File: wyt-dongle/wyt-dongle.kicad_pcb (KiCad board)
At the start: 2 copper layers, 17.2 x 36 mm, 17 parts, among them J1 USB_A, J2 Conn_01x05_Pin, J3 Conn_01x02_Pin, P1 USB_C_Plug_USB2.0, Q1 2N7002, Q2 2N7002, SW1 BOOT, U1 XC6206PxxxMR, U2 ESP32-S2-MINI-2

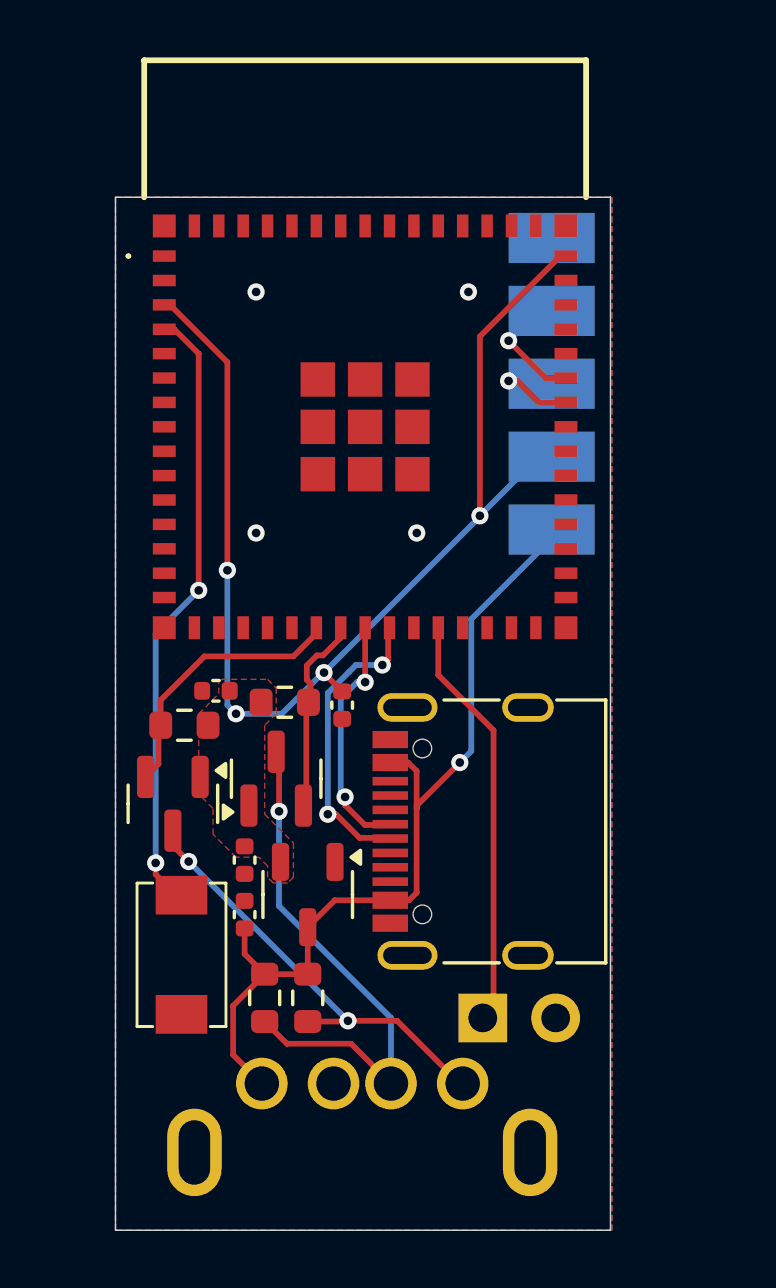
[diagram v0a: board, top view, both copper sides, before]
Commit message: feat: expose more gpios and add reset button
fix: switch to larger LDO

fix: avoid gpio tied to flash for IR LED

fix: connect all usb data pins

fix: add 5.1K resistors for passive usb power
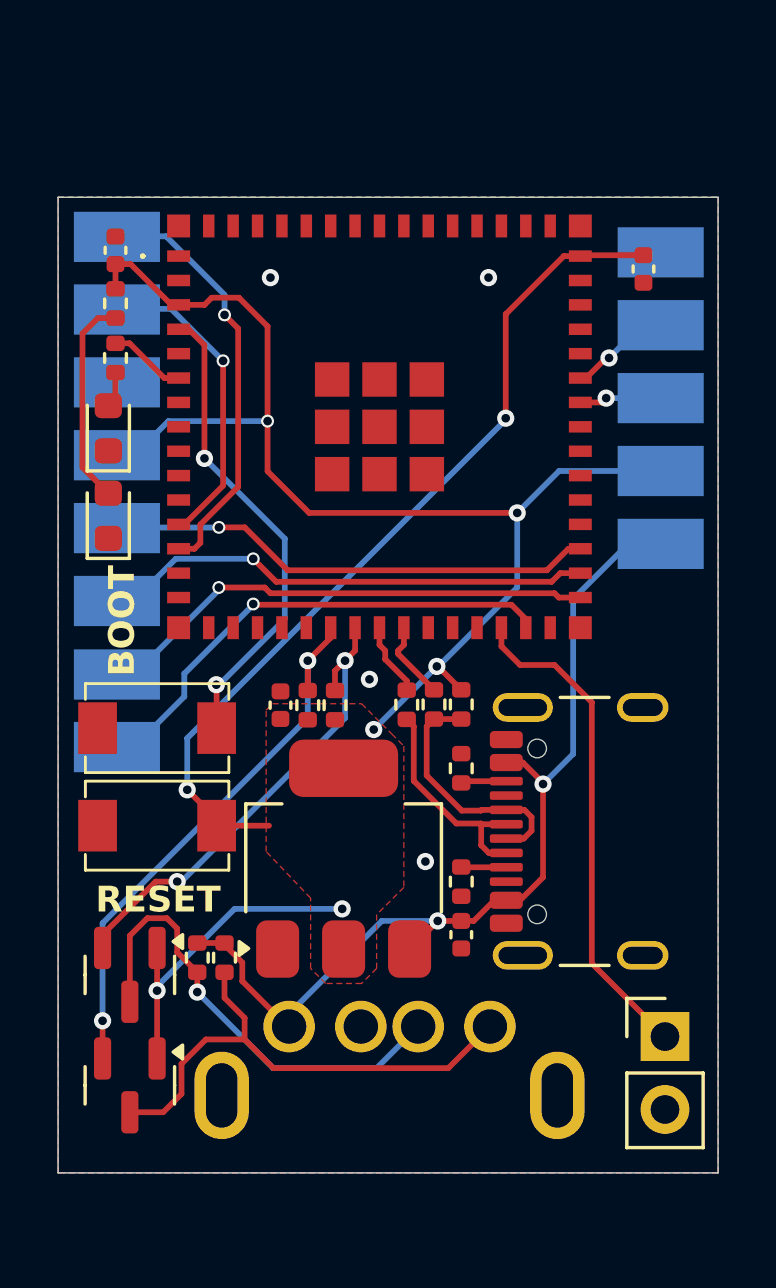
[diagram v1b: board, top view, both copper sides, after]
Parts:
- added D1: Red LED, LED_SMD:LED_0603_1608Metric, F.Cu at (123.8, 63.1)
- added D2: Blue LED, LED_SMD:LED_0603_1608Metric, F.Cu at (123.8, 60.0)
- added J4: Conn_01x08_Pin, Local Library:1x08_Header_Pins_Horizontal, B.Cu at (124.0, 62.3)
- added R10: 0R, Resistor_SMD:R_0402_1005Metric, F.Cu at (135.1, 69.7)
- added R11: 10K, Resistor_SMD:R_0402_1005Metric, F.Cu at (136.1, 69.7)
- added R5: 5.1K, Resistor_SMD:R_0402_1005Metric, F.Cu at (136.1, 75.8)
- added R6: 5.1K, Resistor_SMD:R_0402_1005Metric, F.Cu at (136.1, 71.9)
- added R7: 220R, Resistor_SMD:R_0402_1005Metric, F.Cu at (124.0, 55.7)
- added R8: 220R, Resistor_SMD:R_0402_1005Metric, F.Cu at (124.0, 57.6)
- added R9: 0R, Resistor_SMD:R_0402_1005Metric, F.Cu at (134.2, 69.7)
- added SW1: RESET, Local Library:Xunpu_TS-1088-AR02016, F.Cu at (125.5, 73.9)
- C1, C2: value 1uF -> 10uF
- J1: renamed from J3; moved to F.Cu
- P1: value USB_C_Plug_USB2.0 -> USB_C_Receptacle_USB2.0_16P; footprint Connector_USB:USB_C_Receptacle_G-Switch_GT-USB-7010ASV -> Connector_USB:USB_C_Receptacle_GCT_USB4105-xx-A_16P_TopMnt_Horizontal
- R1, R2, R3, R4: footprint Resistor_SMD:R_0603_1608Metric -> Resistor_SMD:R_0402_1005Metric
- U1: value XC6206PxxxMR -> AMS1117-3.3; footprint Package_TO_SOT_SMD:SOT-23-3 -> Package_TO_SOT_SMD:SOT-223-3_TabPin2
- moved C3 18.5 mm to (142.4, 54.5)
- moved C4 15.7 mm to (124.0, 53.9), turned to 90 degrees
- moved Q1 9.93 mm to (124.5, 83.0)
- moved Q2 8.53 mm to (124.5, 79.1), turned to -90 degrees
- moved SW2 7.95 mm to (125.5, 70.5), turned to 0 degrees
- moved C1 7.58 mm to (136.1, 77.7), turned to -90 degrees
- moved J1 6.38 mm to (143.2, 81.2), turned to 0 degrees
- moved C2 5.54 mm to (129.8, 69.7), turned to 90 degrees
- moved R1 4.36 mm to (130.7, 69.7), turned to 90 degrees
- moved P1 4.00 mm to (141.3, 74.1)
- moved J2 3.83 mm to (143.0, 59.0)
- moved R3 3.22 mm to (127.8, 78.5)
- moved R4 2.74 mm to (126.8, 78.5)
- moved J3 2.20 mm to (137.1, 80.9)
- moved U1 1.77 mm to (131.9, 75.0), turned to 90 degrees
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- renumbered C4 to C3, C3 to C4, J1 to J3, SW1 to SW2
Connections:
- P1 pad A5: unconnected-(P1-CC-PadA5) -> Net-(P1-CC1)
- P1 pad A8: (no net) -> unconnected-(P1-SBU1-PadA8)
- P1 pad B5: unconnected-(P1-VCONN-PadB5) -> Net-(P1-CC2)
- P1 pad B6: (no net) -> /D+
- P1 pad B7: (no net) -> /D-
- P1 pad B8: (no net) -> unconnected-(P1-SBU2-PadB8)
- U2 pad 12: unconnected-(U2-IO8-Pad12) -> /SDA
- U2 pad 13: unconnected-(U2-IO9-Pad13) -> /SCL
- U2 pad 23: /D- -> /D_N
- U2 pad 24: /D+ -> /D_P
- U2 pad 26: /IR -> unconnected-(U2-IO26-Pad26)
- U2 pad 28: unconnected-(U2-IO33-Pad28) -> /IR
- U2 pad 29: unconnected-(U2-IO34-Pad29) -> /CS
- U2 pad 31: unconnected-(U2-IO35-Pad31) -> /MOSI
- U2 pad 32: unconnected-(U2-IO36-Pad32) -> /SCK
- U2 pad 33: unconnected-(U2-IO37-Pad33) -> /MISO
- U2 pad 6: unconnected-(U2-IO2-Pad6) -> Net-(U2-IO2)
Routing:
- net +3.3V: track 41.9 -> 85.7 mm, vias 4 -> 8
- net /MOSI: track 0.00 -> 17.6 mm, vias 0 -> 1
- net /CS: track 0.00 -> 17.3 mm, vias 0 -> 1
- net /SCK: track 0.00 -> 17.2 mm, vias 0 -> 1
- net /MISO: track 0.00 -> 17.1 mm, vias 0 -> 1
- net /SCL: track 0.00 -> 14.8 mm, vias 0 -> 1
- net /SDA: track 0.00 -> 10.9 mm, vias 0 -> 1
- net /TXD: track 9.48 -> 19.3 mm, vias 0 -> 2
- net /RXD: track 6.87 -> 16.5 mm, vias 0 -> 2
- net Net-(D1-A): track 0.00 -> 7.31 mm
- net Net-(U2-IO0): track 21.5 -> 16.7 mm
- net Net-(U2-IO2): track 0.00 -> 2.90 mm
- net /D_P: track 0.00 -> 2.77 mm
- net /IR: track 14.6 -> 17.3 mm
- net /D_N: track 0.00 -> 2.57 mm
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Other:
- board size 17.2 x 36 mm -> 23 x 34 mm
- board text added: "+3.3V"
- board text added: "+5V"
- board text added: "BOOT"
- board text added: "GND"
- board text added: "IO37"
- board text added: "IO38"
- board text added: "IO39"
- board text added: "IO8"
- board text added: "IO9"
- board text added: "IR"
- board text added: "RESET"
- board text added: "RX0"
- board text added: "RX1"
- board text added: "TX0"
- board text added: "TX1"

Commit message: chore: space buttons apart for easier flashing
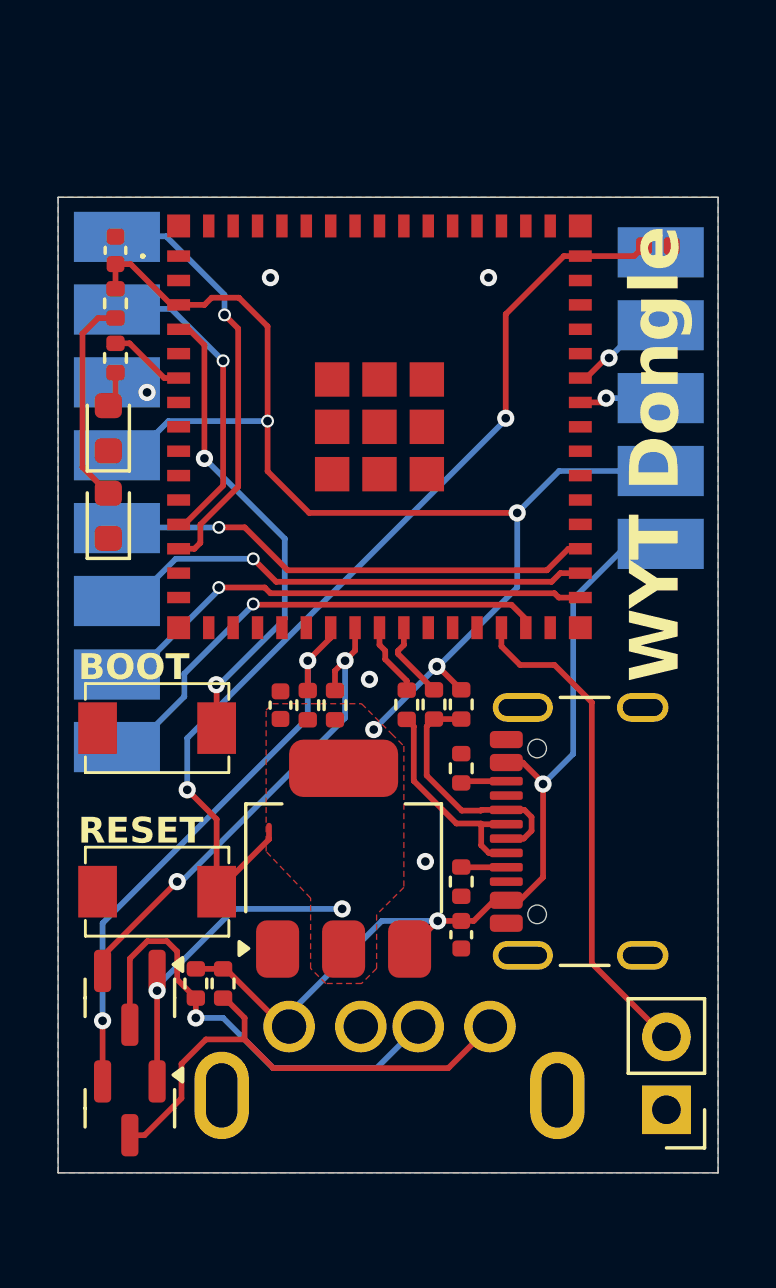
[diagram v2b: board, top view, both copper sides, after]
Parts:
- moved J1 2.55 mm to (143.2, 83.8), turned to 180 degrees
- moved SW1 2.30 mm to (125.5, 76.2)
- moved C3 0.94 mm to (142.9, 53.7), turned to 180 degrees
- moved R3 0.90 mm to (127.8, 79.4)
- moved R4 0.90 mm to (126.8, 79.4)
- moved Q2 0.80 mm to (124.5, 79.9)
- moved Q1 0.80 mm to (124.5, 83.8)
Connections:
- J1 pad 1: /IR -> GND
- J1 pad 2: GND -> /IR
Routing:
- net +3.3V: track 85.7 -> 89.4 mm
- net /TXD: track 19.3 -> 20.1 mm
- net +5V: track 33.2 -> 32.5 mm
- net GND: vias 4 -> 5
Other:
- board text added: "WYT Dongle"
